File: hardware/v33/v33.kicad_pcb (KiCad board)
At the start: 2 copper layers, 99.1 x 99.1 mm, 10 parts, among them J1 nuMezzanine_4x34, U1 uPD70136L-16

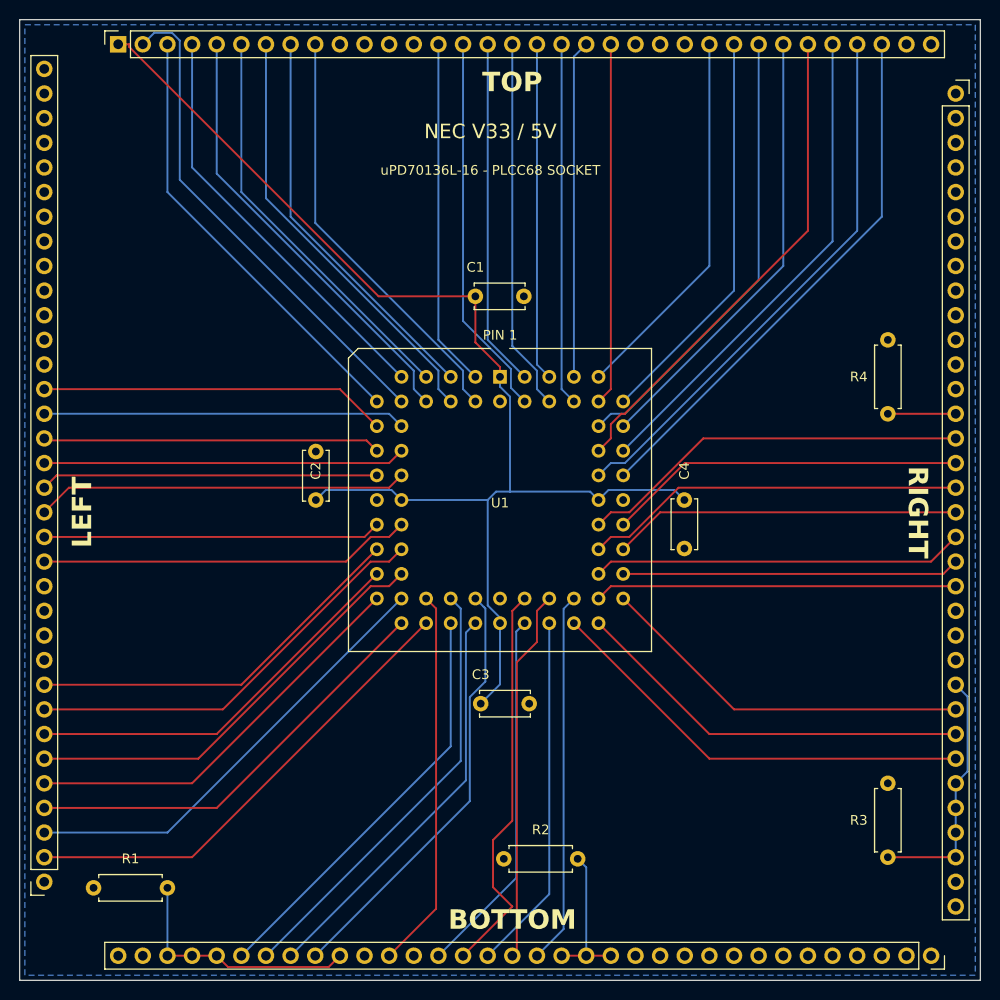
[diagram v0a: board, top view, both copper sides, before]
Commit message: Update mainboard to revision 2
Add an additional 8 bidirectional channels
Replace SPI PSRAM with hyperram
Remove LEDs
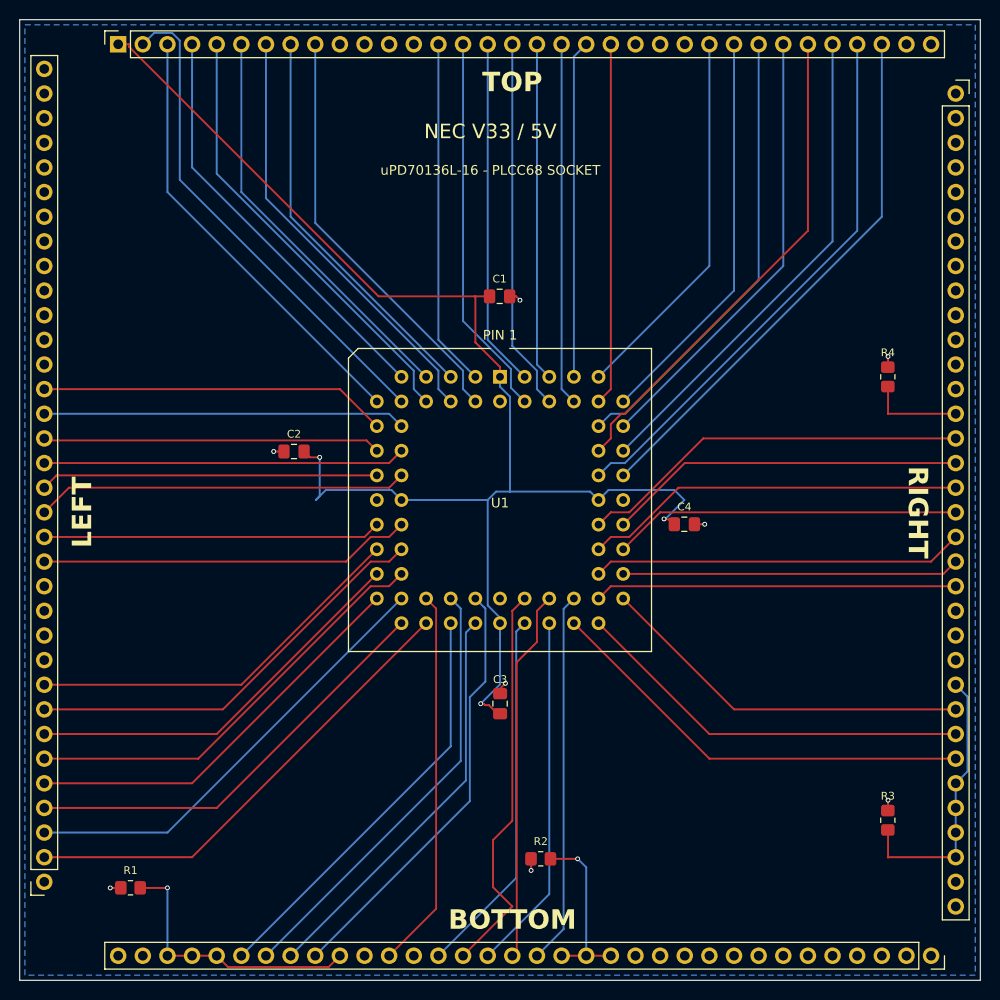
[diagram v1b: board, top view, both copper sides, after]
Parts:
- C1, C2, C3, C4: footprint Capacitor_THT:C_Disc_D5.0mm_W2.5mm_P5.00mm -> Capacitor_SMD:C_0805_2012Metric_Pad1.18x1.45mm_HandSolder
- R1, R2, R3, R4: footprint Resistor_THT:R_Axial_DIN0207_L6.3mm_D2.5mm_P7.62mm_Horizontal -> Resistor_SMD:R_0805_2012Metric_Pad1.20x1.40mm_HandSolder
- moved C2 5.48 mm to (129.8, 91.0), turned to 180 degrees
- moved R1 3.81 mm to (112.9, 136.0)
- moved R2 3.81 mm to (155.2, 133.0)
- moved R3 3.81 mm to (191.0, 129.0)
- moved R4 3.81 mm to (191.0, 83.3)
- moved C1 2.50 mm to (150.9, 75.0)
- moved C4 2.50 mm to (170.0, 98.5), turned to 0 degrees
- moved C3 2.00 mm to (151.0, 117.0), turned to 90 degrees
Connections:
- J1 pad 10: GND -> unconnected-(J1A-TX3-Pad10)
- J1 pad 102: unconnected-(J1E-NC-Pad102) -> GND
- J1 pad 112: GND -> unconnected-(J1B-LX3-Pad112)
- J1 pad 115: GND -> unconnected-(J1B-LX0-Pad115)
- J1 pad 13: GND -> unconnected-(J1A-TX0-Pad13)
- J1 pad 136: unconnected-(J1E-NC-Pad136) -> GND
- J1 pad 44: GND -> unconnected-(J1D-RX3-Pad44)
- J1 pad 47: GND -> unconnected-(J1D-RX0-Pad47)
- J1 pad 78: GND -> unconnected-(J1C-BX3-Pad78)
- J1 pad 81: GND -> unconnected-(J1C-BX0-Pad81)
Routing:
- net /VCC_TL: track 132.2 -> 146.7 mm, vias 0 -> 3
- net GND: track 0.00 -> 9.17 mm, vias 0 -> 8
- net /R0_UNUSED: track 25.8 -> 28.7 mm
- net /R1_UNUSED: track 7.00 -> 9.84 mm
- net /B0_UNUSED: track 25.7 -> 28.6 mm, vias 0 -> 1
- net /B1_UNUSED: track 15.4 -> 18.2 mm, vias 0 -> 1
